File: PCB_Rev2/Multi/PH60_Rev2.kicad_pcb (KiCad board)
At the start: 2 copper layers, 285 x 94.6 mm, 182 parts, among them J1 USB_C_Receptacle_USB2.0_16P, J2 Conn_01x02, U2 W25Q128JVS, U3 RP2040, U4 XC6206PxxxMR, Y1 Crystal_GND24

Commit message: Wiring and Ground Connection Improvement
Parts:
- moved J2 0.51 mm to (115.8, 110.3)
- moved C4 0.27 mm to (113.3, 113.5), turned to 90 degrees
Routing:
- net col_10: track 207.2 -> 186.5 mm
- net col_13: track 343.0 -> 332.8 mm
- net col_11: track 244.5 -> 234.3 mm
- net col_12: track 275.9 -> 265.7 mm
- net GND: track 57.4 -> 47.4 mm, vias 21 -> 23
- net col_9: track 158.6 -> 165.0 mm
- net col_6: track 138.5 -> 132.6 mm
- net row_3: track 303.6 -> 297.9 mm
- net row_2: track 334.2 -> 330.2 mm
- net row_0: track 397.5 -> 395.9 mm
- net row_4: track 269.8 -> 269.1 mm
- net row_1: track 372.0 -> 371.4 mm
- net +3V3: track 93.8 -> 93.4 mm, vias 5 -> 4

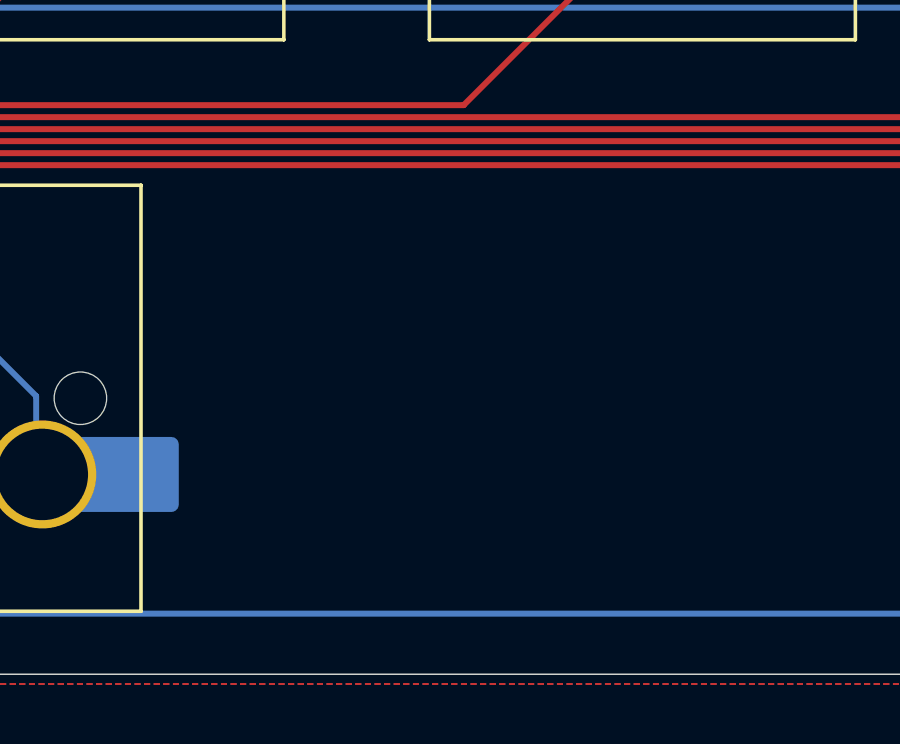
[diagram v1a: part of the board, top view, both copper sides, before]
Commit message: Schematic Tinkering and RF Module Placing
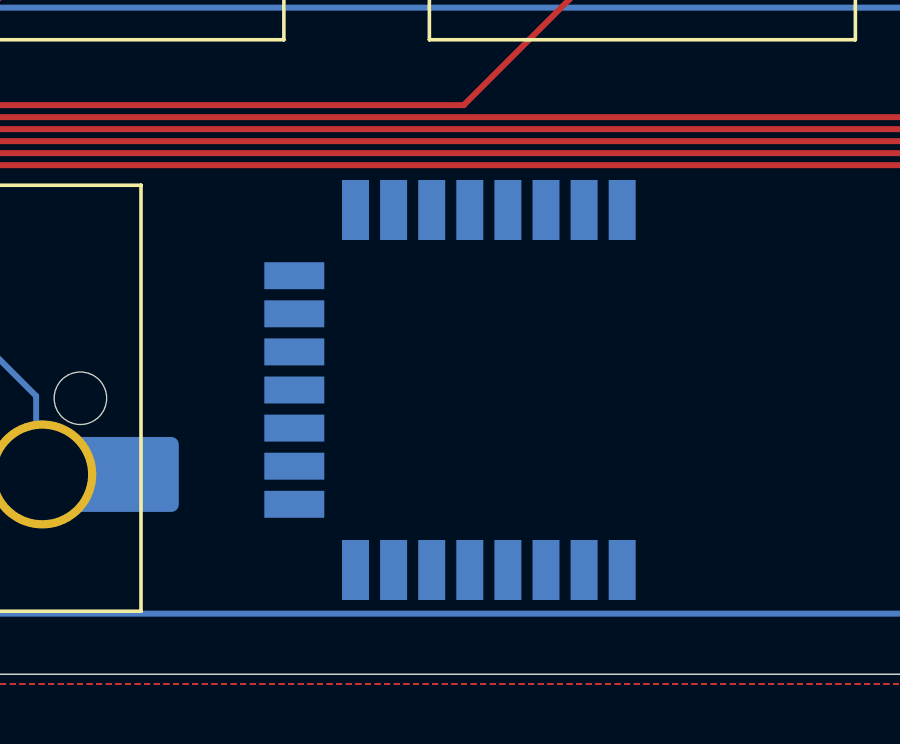
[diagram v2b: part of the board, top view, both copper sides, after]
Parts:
- added U1: ~, nRF_Module:nRF52810_Module, B.Cu at (193.5, 114.0)

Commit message: Multi PCB Rework
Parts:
- removed the S14 at (285.8, 38.1)
- removed the S28 at (281.0, 76.2)
- removed the S28 at (300.0, 57.1)
- removed the S29 at (40.5, 76.2)
- removed the S41 at (302.4, 66.7)
- removed the S41 at (292.9, 76.2)
- removed the S43 at (50.0, 95.2)
- removed the S56 at (288.1, 95.2)
- removed the S57 at (42.9, 114.3)
- removed the S58 at (66.7, 114.3)
- removed the S59 at (90.5, 114.3)
- removed the S60 at (171.4, 114.3)
- removed the S62 at (252.4, 114.3)
- removed the S63 at (276.2, 114.3)
- removed the S64 at (300.0, 114.3)
- removed U1: ~, nRF_Module:nRF52810_Module
- added S14-2: MX1A, PCM_Switch_Keyboard_Hotswap_Kailh:SW_Hotswap_Kailh_MX_Plated_1.00u, F.Cu at (285.8, 38.1)
- added S28: MX1A, PCM_Switch_Keyboard_Hotswap_Kailh:SW_Hotswap_Kailh_MX_Plated_ISOEnter_90deg, F.Cu at (302.4, 66.7)
- added S28-2: MX1A, PCM_Switch_Keyboard_Hotswap_Kailh:SW_Hotswap_Kailh_MX_Plated_2.25u_90deg, F.Cu at (292.9, 76.2)
- added S29-2: MX1A, PCM_Switch_Keyboard_Hotswap_Kailh:SW_Hotswap_Kailh_MX_Plated_1.25u_90deg, F.Cu at (40.5, 76.2)
- added S41: MX1A, PCM_Switch_Keyboard_Hotswap_Kailh:SW_Hotswap_Kailh_MX_Plated_1.00u, F.Cu at (281.0, 76.2)
- added S41-2: MX1A, PCM_Switch_Keyboard_Hotswap_Kailh:SW_Hotswap_Kailh_MX_Plated_1.50u_90deg, F.Cu at (300.0, 57.1)
- added S43-2: MX1A, PCM_Switch_Keyboard_Hotswap_Kailh:SW_Hotswap_Kailh_MX_Plated_2.25u, F.Cu at (50.0, 95.2)
- added S55-2: MX1A, PCM_Switch_Keyboard_Hotswap_Kailh:SW_Hotswap_Kailh_MX_Plated_2.75u_90deg, F.Cu at (288.1, 95.2)
- added S57-2: MX1A, PCM_Switch_Keyboard_Hotswap_Kailh:SW_Hotswap_Kailh_MX_Plated_1.50u_90deg, F.Cu at (42.9, 114.3)
- added S58-2: MX1A, PCM_Switch_Keyboard_Hotswap_Kailh:SW_Hotswap_Kailh_MX_Plated_1.00u, F.Cu at (66.7, 114.3)
- added S59-2: MX1A, PCM_Switch_Keyboard_Hotswap_Kailh:SW_Hotswap_Kailh_MX_Plated_1.50u_90deg, F.Cu at (90.5, 114.3)
- added S60-2: MX1A, PCM_Switch_Keyboard_Hotswap_Kailh:SW_Hotswap_Kailh_MX_Plated_7.00u, F.Cu at (171.4, 114.3)
- added S62-2: MX1A, PCM_Switch_Keyboard_Hotswap_Kailh:SW_Hotswap_Kailh_MX_Plated_1.50u_90deg, F.Cu at (252.4, 114.3)
- added S63-2: MX1A, PCM_Switch_Keyboard_Hotswap_Kailh:SW_Hotswap_Kailh_MX_Plated_1.00u, F.Cu at (276.2, 114.3)
- added S64-2: MX1A, PCM_Switch_Keyboard_Hotswap_Kailh:SW_Hotswap_Kailh_MX_Plated_1.50u_90deg, F.Cu at (300.0, 114.3)
- J2: footprint Connector_PinHeader_2.54mm:PinHeader_1x02_P2.54mm_Vertical -> Connector_PinHeader_1.27mm:PinHeader_1x02_P1.27mm_Vertical
- U2: footprint Package_SO:SOIC-8_5.23x5.23mm_P1.27mm -> Package_SON:Winbond_USON-8-1EP_3x2mm_P0.5mm_EP0.2x1.6mm
- moved J2 192.1 mm to (-30.2, -14.4), turned to 180 degrees
- moved D58 22.9 mm to (76.7, 107.3)
- moved D59 22.9 mm to (100.5, 107.3)
- moved C14 18.5 mm to (136.9, 109.4), turned to 90 degrees
- moved D43 17.3 mm to (67.0, 98.5), turned to 90 degrees
- moved C1 17.3 mm to (122.7, 110.0)
- moved U4 17.0 mm to (125.3, 109.5)
- moved D42 15.9 mm to (284.0, 57.1), turned to 90 degrees
- moved C5 15.4 mm to (124.7, 114.0), turned to 180 degrees
- moved C4 15.0 mm to (127.9, 110.0)
- moved C9 14.6 mm to (131.1, 120.0), turned to -90 degrees
- moved C16 12.6 mm to (126.2, 115.5)
- moved C12 11.2 mm to (136.4, 120.2), turned to 180 degrees
- moved D55 9.97 mm to (266.6, 98.5), turned to 90 degrees
- moved D57 9.55 mm to (52.9, 107.3)
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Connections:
- U3 pad 27: row_2 -> unconnected-(U3-GPIO16-Pad27)
- U3 pad 28: row_3 -> unconnected-(U3-GPIO17-Pad28)
- U3 pad 29: row_4 -> row_2
- U3 pad 30: unconnected-(U3-GPIO19-Pad30) -> row_3
- U3 pad 31: unconnected-(U3-GPIO20-Pad31) -> row_4
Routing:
- net /USB_D-: track 165.8 -> 4.52 mm
- net /USB_D+: track 165.8 -> 5.44 mm
- net row_0: track 395.9 -> 247.3 mm, vias 2 -> 0
- net row_4: track 269.1 -> 120.8 mm
- net VBUS: track 152.8 -> 7.99 mm, vias 2 -> 1
- net row_1: track 371.4 -> 244.6 mm, vias 2 -> 0
- net row_2: track 330.2 -> 244.5 mm, vias 4 -> 0
- net row_3: track 297.9 -> 236.4 mm, vias 2 -> 0
- net col_12: track 265.7 -> 311.2 mm
- net Net-(D28-A): track 77.4 -> 35.5 mm
- net GND: track 47.4 -> 9.22 mm, vias 23 -> 4
- net +3V3: track 93.4 -> 60.8 mm, vias 4 -> 2
- net Net-(D41-A): track 31.0 -> 53.1 mm
- net Net-(D55-A): track 8.12 -> 26.3 mm
- net /~{USB_BOOT}: track 18.1 -> 0.00 mm, vias 1 -> 0
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- removed copper zone on B.Cu, net GND
- removed copper zone on F.Cu, net GND

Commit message: Multi PCB Wiring
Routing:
- net col_2: track 155.8 -> 148.7 mm
- net col_1: track 172.3 -> 179.4 mm
- net col_0: track 204.1 -> 209.7 mm
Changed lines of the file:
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@@
+	)
+	(segment
+		(start 94.938035 121.005)
+		(end 55.9175 121.005)
+		(width 0.2)
+		(layer "F.Cu")
+		(net 87)
 	)
 	(segment
 		(start 130.49 108.05)
-		(end 130.29 107.85)
+		(end 126.1711 103.7311)
 		(width 0.2)
 		(layer "F.Cu")
@@
 	)
 	(segment
+		(start 126.1711 103.7311)
+		(end 108.572875 103.7311)
+		(width 0.2)
+		(layer "F.Cu")
+		(net 87)
+	)
+	(segment
 		(start 47.46625 100.33)
 		(end 47.46625 108.42625)
@@
 	)
 	(segment
-		(start 107.173514 121.005)
-		(end 55.9175 121.005)
+		(start 98.0675 117.875535)
+		(end 94.938035 121.005)
 		(width 0.2)
 		(layer "F.Cu")
@@
 	)
 	(segment
-		(start 130.29 107.85)
-		(end 120.328514 107.85)
-		(width 0.2)
-		(layer "F.Cu")
-		(net 87)
-	)
-	(segment
 		(start 44.45 52.07)
 		(end 45.4025 52.07)
@@
 	)
 	(segment
+		(start 108.572875 103.7311)
+		(end 98.0675 114.236475)
+		(width 0.2)
+		(layer "F.Cu")
+		(net 87)
+	)
+	(segment
 		(start 35.56 43.18)
 		(end 44.45 52.07)
@@
 	)
 	(segment
-		(start 120.328514 107.85)
-		(end 107.173514 121.005)
+		(start 98.0675 114.236475)
+		(end 98.0675 117.875535)
 		(width 0.2)
 		(layer "F.Cu")
@@
 	)
 	(segment
-		(start 120.162828 107.45)
-		(end 107.007828 120.605)
+		(start 97.6675 114.070789)
+		(end 97.6675 117.709849)
+		(width 0.2)
+		(layer "F.Cu")
+		(net 88)
+	)
+	(segment
+		(start 64.4525 106.52125)
+		(end 59.21375 111.76)
 		(width 0.2)
 		(layer "F.Cu")
@@
 	)
 	(segment
-		(start 130.738529 107.45)
-		(end 120.162828 107.45)
+		(start 131.29 108.05)
+		(end 131.29 108.001471)
+		(width 0.2)
+		(layer "F.Cu")
+		(net 88)
+	)
+	(segment
+		(start 108.407189 103.3311)
+		(end 97.6675 114.070789)
+		(width 0.2)
+		(layer "F.Cu")
+		(net 88)
+	)
+	(segment
+		(start 94.772349 120.605)
+		(end 79.33 120.605)
+		(width 0.2)
+		(layer "F.Cu")
+		(net 88)
+	)
+	(segment
+		(start 97.6675 117.709849)
+		(end 94.772349 120.605)
 		(width 0.2)
 		(layer "F.Cu")
@@
 	)
 	(segment
-		(start 131.29 108.05)
-		(end 131.29 108.001471)
+		(start 64.4525 90.17)
+		(end 64.4525 106.52125)
+		(width 0.2)
+		(layer "F.Cu")
+		(net 88)
+	)
+	(segment
+		(start 126.619629 103.3311)
+		(end 108.407189 103.3311)
 		(width 0.2)
 		(layer "F.Cu")
@@
 	)
 	(segment
-		(start 69.215 94.9325)
-		(end 64.4525 90.17)
-		(width 0.2)
-		(layer "F.Cu")
-		(net 88)
-	)
-	(segment
 		(start 131.29 108.001471)
-		(end 130.738529 107.45)
-		(width 0.2)
-		(layer "F.Cu")
-		(net 88)
-	)
-	(segment
-		(start 69.215 110.49)
-		(end 69.215 94.9325)
-		(width 0.2)
-		(layer "F.Cu")
-		(net 88)
-	)
-	(segment
-		(start 107.007828 120.605)
-		(end 79.33 120.605)
+		(end 126.619629 103.3311)
 		(width 0.2)
 		(layer "F.Cu")
@@
 	)
 	(segment
+		(start 132.09 108.05)
+		(end 132.09 108.001471)
+		(width 0.2)
+		(layer "F.Cu")
+		(net 89)
+	)
+	(segment
 		(start 88.265 66.3575)
 		(end 93.0275 71.12)
@@
 	)
 	(segment
-		(start 131.138529 107.05)
-		(end 119.997142 107.05)
-		(width 0.2)
-		(layer "F.Cu")
-		(net 89)
-	)
-	(segment
 		(start 88.265 52.07)
 		(end 88.265 42.545)
@@
 	)
 	(segment
-		(start 132.09 108.001471)
-		(end 131.138529 107.05)
-		(width 0.2)
-		(layer "F.Cu")
-		(net 89)
-	)
-	(segment
-		(start 93.0275 110.49)
-		(end 93.0275 99.695)
-		(width 0.2)
-		(layer "F.Cu")
-		(net 89)
-	)
-	(segment
-		(start 106.842142 120.205)
-		(end 102.7425 120.205)
-		(width 0.2)
-		(layer "F.Cu")
-		(net 89)
-	)
-	(segment
 		(start 88.265 52.07)
 		(end 88.265 66.3575)
@@
 	)
 	(segment
-		(start 119.997142 107.05)
-		(end 106.842142 120.205)
-		(width 0.2)
-		(layer "F.Cu")
-		(net 89)
-	)
-	(segment
-		(start 132.09 108.05)
-		(end 132.09 108.001471)
-		(width 0.2)
-		(layer "F.Cu")
-		(net 89)
-	)
-	(segment
-		(start 102.7425 120.205)
-		(end 93.0275 110.49)
+		(start 132.09 108.001471)
+		(end 127.019629 102.9311)
+		(width 0.2)
+		(layer "F.Cu")
+		(net 89)
+	)
+	(segment
+		(start 83.5025 111.28375)
+		(end 83.02625 111.76)
+		(width 0.2)
+		(layer "F.Cu")
+		(net 89)
+	)
+	(segment
+		(start 108.241503 102.9311)
+		(end 100.682603 110.49)
+		(width 0.2)
+		(layer "F.Cu")
+		(net 89)
+	)
+	(segment
+		(start 83.5025 90.17)
+		(end 83.5025 111.28375)
 		(width 0.2)
 		(layer "F.Cu")
@@
 	)
 	(segment
+		(start 127.019629 102.9311)
+		(end 108.241503 102.9311)
+		(width 0.2)
+		(layer "F.Cu")
+		(net 89)
+	)
+	(segment
 		(start 88.265 42.545)
 		(end 78.74 33.02)
@@
 	)
 	(segment
-		(start 93.0275 99.695)
-		(end 83.5025 90.17)
+		(start 100.682603 110.49)
+		(end 93.0275 110.49)
 		(width 0.2)
 		(layer "F.Cu")
@@
 	)
 	(segment
+		(start 114.9136 102.5311)
+		(end 102.5525 90.17)
+		(width 0.2)
+		(layer "F.Cu")
+		(net 90)
+	)
+	(segment
 		(start 112.0775 80.645)
 		(end 102.5525 90.17)
@@
 	)
 	(segment
+		(start 107.315 42.545)
+		(end 97.79 33.02)
+		(width 0.2)
+		(layer "F.Cu")
+		(net 90)
+	)
+	(segment
+		(start 107.315 52.07)
+		(end 107.315 42.545)
+		(width 0.2)
+		(layer "F.Cu")
+		(net 90)
+	)
+	(segment
+		(start 127.419629 102.5311)
+		(end 114.9136 102.5311)
+		(width 0.2)
+		(layer "F.Cu")
+		(net 90)
+	)
+	(segment
+		(start 132.89 108.001471)
+		(end 127.419629 102.5311)
+		(width 0.2)
+		(layer "F.Cu")
+		(net 90)
+	)
+	(segment
+		(start 112.0775 71.12)
+		(end 112.0775 80.645)
+		(width 0.2)
+		(layer "F.Cu")
+		(net 90)
+	)
+	(segment
 		(start 132.89 108.05)
 		(end 132.89 108.001471)
-		(width 0.2)
-		(layer "F.Cu")
-		(net 90)
-	)
-	(segment
-		(start 109.9825 97.6)
-		(end 102.5525 90.17)
-		(width 0.2)
-		(layer "F.Cu")
-		(net 90)
-	)
-	(segment
-		(start 107.315 42.545)
-		(end 97.79 33.02)
-		(width 0.2)
-		(layer "F.Cu")
-		(net 90)
-	)
-	(segment
-		(start 107.315 52.07)
-		(end 107.315 42.545)
-		(width 0.2)
-		(layer "F.Cu")
-		(net 90)
-	)
-	(segment
-		(start 122.488529 97.6)
-		(end 109.9825 97.6)
-		(width 0.2)
-		(layer "F.Cu")
-		(net 90)
-	)
-	(segment
-		(start 132.89 108.001471)
-		(end 122.488529 97.6)
-		(width 0.2)
-		(layer "F.Cu")
-		(net 90)
-	)
-	(segment
-		(start 112.0775 71.12)
-		(end 112.0775 80.645)
 		(width 0.2)
 		(layer "F.Cu")
@@
 	)
 	(segment
+		(start 133.69 108.05)
+		(end 133.69 108.001471)
+		(width 0.2)
+		(layer "F.Cu")
+		(net 91)
+	)
+	(segment
+		(start 121.6025 95.913971)
+		(end 121.6025 90.17)
+		(width 0.2)
+		(layer "F.Cu")
+		(net 91)
+	)
+	(segment
 		(start 126.365 52.07)
 		(end 126.365 42.545)
@@
 	)
 	(segment
+		(start 133.69 108.001471)
+		(end 121.6025 95.913971)
+		(width 0.2)
+		(layer "F.Cu")
+		(net 91)
+	)
+	(segment
 		(start 126.365 42.545)
 		(end 116.84 33.02)
@@
 	)
 	(segment
-		(start 133.69 108.05)
-		(end 133.69 102.2575)
-		(width 0.2)
-		(layer "F.Cu")
-		(net 91)
-	)
-	(segment
 		(start 126.365 66.3575)
 		(end 131.1275 71.12)
@@
 		(end 121.6025 90.17)
 		(width 0.2)
-		(layer "F.Cu")
-		(net 91)
-	)
-	(segment
-		(start 133.69 102.2575)
-		(end 121.6025 90.17)
-		(width 0.2)

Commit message: Tinkering of Multi PCB
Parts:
- moved J2 195.9 mm to (124.2, 106.2), turned to 90 degrees
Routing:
- net /USB_D-: track 4.52 -> 164.6 mm
- net /USB_D+: track 5.44 -> 164.6 mm
- net VBUS: track 7.99 -> 165.2 mm, vias 1 -> 2
- net row_4: track 120.8 -> 256.7 mm
- net row_0: track 247.3 -> 323.8 mm, vias 0 -> 2
- net row_1: track 244.6 -> 302.8 mm, vias 0 -> 2
- net row_2: track 244.5 -> 292.7 mm, vias 0 -> 2
- net GND: track 9.22 -> 49.6 mm, vias 4 -> 15
- net row_3: track 236.4 -> 266.1 mm
- net col_6: track 121.7 -> 133.4 mm, vias 1 -> 2
- net /~{USB_BOOT}: track 0.00 -> 7.07 mm
- net col_3: track 109.7 -> 113.7 mm
- net +3V3: track 60.8 -> 62.7 mm, vias 2 -> 3
- added copper zone on B.Cu, net GND
- added copper zone on F.Cu, net GND
